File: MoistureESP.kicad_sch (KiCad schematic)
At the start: 10 parts, among them J1 Conn_01x02_Pin, J2 Conn_MoisturePCB, J3 Conn_DS18B20, J4 Conn_01x06_Pin, J5 Conn_01x03_Pin, J6 Conn_01x04_Pin, SW1 147873-1

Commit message: Refine VBAT zone and add wiring under MCU.
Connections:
- net GNDD: now also J4.2 (Pin_2)
- net GNDPWR: no longer J4.2 (Pin_2)
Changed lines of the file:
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@@
 	(wire
 		(pts
-			(xy 52.07 160.02) (xy 52.07 163.83)
+			(xy 52.07 160.02) (xy 52.07 162.56)
 		)
 		(stroke
@@
 	)
 	(symbol
-		(lib_id "power:GNDPWR")
-		(at 52.07 163.83 0)
-		(unit 1)
-		(body_style 1)
-		(exclude_from_sim no)
-		(in_bom yes)
-		(on_board yes)
-		(in_pos_files yes)
-		(dnp no)
-		(fields_autoplaced yes)
-		(property "Reference" "#PWR06"
-			(at 52.07 168.91 0)
-			(hide yes)
-			(show_name no)
-			(do_not_autoplace no)
-			(effects
-				(font
-					(size 1.27 1.27)
-				)
-			)
-		)
-		(property "Value" "GNDPWR"
-			(at 51.943 167.64 0)
-			(show_name no)
-			(do_not_autoplace no)
-			(effects
-				(font
-					(size 1.27 1.27)
-				)
-			)
-		)
-		(property "Footprint" ""
-			(at 52.07 165.1 0)
-			(hide yes)
-			(show_name no)
-			(do_not_autoplace no)
-			(effects
-				(font
-					(size 1.27 1.27)
-				)
-			)
-		)
-		(property "Datasheet" ""
-			(at 52.07 165.1 0)
-			(hide yes)
-			(show_name no)
-			(do_not_autoplace no)
-			(effects
-				(font
-					(size 1.27 1.27)
-				)
-			)
-		)
-		(property "Description" "Power symbol creates a global label with name \"GNDPWR\" , global ground"
-			(at 52.07 163.83 0)
-			(hide yes)
-			(show_name no)
-			(do_not_autoplace no)
-			(effects
-				(font
-					(size 1.27 1.27)
-				)
-			)
-		)
-		(pin "1"
-		)
-		(instances
-			(project "MoistureESP"
-				(path "/f2b9f638-139e-46ec-aa60-77c4af989196"
-					(reference "#PWR06")
-					(unit 1)
-				)
-			)
-		)
-	)
-	(symbol
 		(lib_id "power:GNDD")
 		(at 266.7 96.52 0)
@@
 					(unit 1)
 				)
+			)
+		)
+	)
+	(symbol
+		(lib_id "power:GNDD")
+		(at 52.07 162.56 0)
+		(unit 1)
+		(body_style 1)
+		(exclude_from_sim no)
+		(in_bom yes)
+		(on_board yes)
+		(in_pos_files yes)
+		(dnp no)
+		(fields_autoplaced yes)
+		(property "Reference" "#PWR070"
+			(at 52.07 168.91 0)
+			(hide yes)
+			(show_name no)
+			(do_not_autoplace no)
+			(effects
+				(font
+					(size 1.27 1.27)
+				)
+			)
+		)
+		(property "Value" "GNDD"
+			(at 52.07 166.37 0)
+			(show_name no)
+			(do_not_autoplace no)
+			(effects
+				(font
+					(size 1.27 1.27)
+				)
+			)
+		)
+		(property "Footprint" ""
+			(at 52.07 162.56 0)
+			(hide yes)
+			(show_name no)
+			(do_not_autoplace no)
+			(effects
+				(font
+					(size 1.27 1.27)
+				)
+			)
+		)
+		(property "Datasheet" ""
+			(at 52.07 162.56 0)
+			(hide yes)
+			(show_name no)
+			(do_not_autoplace no)
+			(effects
+				(font
+					(size 1.27 1.27)
+				)
+			)
+		)
+		(property "Description" "Power symbol creates a global label with name \"GNDD\" , digital ground"
+			(at 52.07 162.56 0)
+			(hide yes)
+			(show_name no)
+			(do_not_autoplace no)
+			(effects
+				(font
+					(size 1.27 1.27)
+				)
+			)
+		)
+		(pin "1"
+		)
+		(instances
+			(project "MoistureESP"
+				(path "/f2b9f638-139e-46ec-aa60-77c4af989196"
+					(reference "#PWR070")
+					(unit 1)
+				)

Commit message: Fix ESP32 GPIO wiring, many bootstrap pins were used.
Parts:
- J6: footprint (none) -> Connector_PinHeader_2.54mm:PinHeader_1x04_P2.54mm_Vertical
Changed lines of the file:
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@@
 			)
 		)
-		(property "Footprint" ""
+		(property "Footprint" "Connector_PinHeader_2.54mm:PinHeader_1x04_P2.54mm_Vertical"
 			(at 278.13 90.17 0)
 			(hide yes)

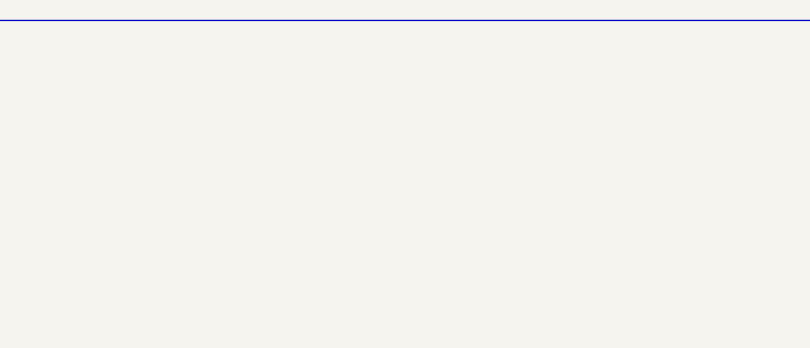
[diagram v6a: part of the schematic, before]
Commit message: Editing layout, redrawing analog and RTS DTS signals. Placing the silk layer designators
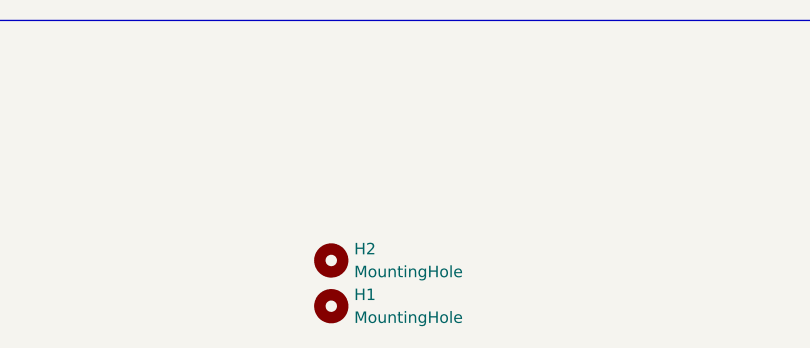
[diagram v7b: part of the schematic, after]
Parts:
- added H1, H2: MountingHole, MountingHole:MountingHole_2.7mm_M2.5_DIN965, symbol Mechanical:MountingHole
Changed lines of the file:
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@@
+	)
+	(symbol
+		(lib_id "Mechanical:MountingHole")
+		(at 132.08 186.69 0)
+		(unit 1)
+		(body_style 1)
+		(exclude_from_sim no)
+		(in_bom no)
+		(on_board yes)
+		(in_pos_files yes)
+		(dnp no)
+		(fields_autoplaced yes)
+		(property "Reference" "H2"
+			(at 134.62 185.4199 0)
+			(show_name no)
+			(do_not_autoplace no)
+			(effects
+				(font
+					(size 1.27 1.27)
+				)
+				(justify left)
+			)
+		)
+		(property "Value" "MountingHole"
+			(at 134.62 187.9599 0)
+			(show_name no)
+			(do_not_autoplace no)
+			(effects
+				(font
+					(size 1.27 1.27)
+				)
+				(justify left)
+			)
+		)
+		(property "Footprint" "MountingHole:MountingHole_2.7mm_M2.5_DIN965"
+			(at 132.08 186.69 0)
+			(hide yes)
+			(show_name no)
+			(do_not_autoplace no)
+			(effects
+				(font
+					(size 1.27 1.27)
+				)
+			)
+		)
+		(property "Datasheet" ""
+			(at 132.08 186.69 0)
+			(hide yes)
+			(show_name no)
+			(do_not_autoplace no)
+			(effects
+				(font
+					(size 1.27 1.27)
+				)
+			)
+		)
+		(property "Description" "Mounting Hole without connection"
+			(at 132.08 186.69 0)
+			(hide yes)
+			(show_name no)
+			(do_not_autoplace no)
+			(effects
+				(font
+					(size 1.27 1.27)
+				)
+			)
+		)
+		(instances
+			(project "MoistureESP"
+				(path "/f2b9f638-139e-46ec-aa60-77c4af989196"
+					(reference "H2")
+					(unit 1)
+				)
+			)
+		)
 	)
 	(symbol
@@
 					(unit 1)
 				)
+			)
+		)
+	)
+	(symbol
+		(lib_id "Mechanical:MountingHole")
+		(at 132.08 191.77 0)
+		(unit 1)
+		(body_style 1)
+		(exclude_from_sim no)
+		(in_bom no)
+		(on_board yes)
+		(in_pos_files yes)
+		(dnp no)
+		(fields_autoplaced yes)
+		(property "Reference" "H1"
+			(at 134.62 190.4999 0)
+			(show_name no)
+			(do_not_autoplace no)
+			(effects
+				(font
+					(size 1.27 1.27)
+				)
+				(justify left)
+			)
+		)
+		(property "Value" "MountingHole"
+			(at 134.62 193.0399 0)
+			(show_name no)
+			(do_not_autoplace no)
+			(effects
+				(font
+					(size 1.27 1.27)
+				)
+				(justify left)
+			)
+		)
+		(property "Footprint" "MountingHole:MountingHole_2.7mm_M2.5_DIN965"
+			(at 132.08 191.77 0)
+			(hide yes)
+			(show_name no)
+			(do_not_autoplace no)
+			(effects
+				(font
+					(size 1.27 1.27)
+				)
+			)
+		)
+		(property "Datasheet" ""
+			(at 132.08 191.77 0)
+			(hide yes)
+			(show_name no)
+			(do_not_autoplace no)
+			(effects
+				(font
+					(size 1.27 1.27)
+				)
+			)
+		)
+		(property "Description" "Mounting Hole without connection"
+			(at 132.08 191.77 0)
+			(hide yes)
+			(show_name no)
+			(do_not_autoplace no)
+			(effects
+				(font
+					(size 1.27 1.27)
+				)
+			)
+		)
+		(instances
+			(project "MoistureESP"
+				(path "/f2b9f638-139e-46ec-aa60-77c4af989196"
+					(reference "H1")
+					(unit 1)
+				)

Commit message: Export BOM, change page headers.
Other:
- company: (none) -> B.Major
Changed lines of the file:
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@@
 	(generator_version "10.0")
 	(paper "A4")
+	(title_block
+		(date "2026-03-27")
+		(rev "1")
+		(company "B.Major")
+	)
 	(text "Vsys connection for charger module, or further development."
 		(exclude_from_sim no)
